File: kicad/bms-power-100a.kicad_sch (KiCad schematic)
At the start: 47 parts, among them P1 CONN_01X01, P2 CONN_01X01, P3 CONN_01X01, P4 CONN_01X01, Q1 Q_NMOS_GDS, Q10 Q_NMOS_GDS, Q11 Q_NMOS_GDS, Q12 Q_NMOS_GDS, Q13 Q_NMOS_GDS, Q14 Q_NMOS_GDS, Q15 Q_NMOS_GDS, Q16 Q_NMOS_GDS, Q17 Q_NMOS_GDS, Q18 Q_NMOS_GDS, Q19 Q_NMOS_GDS, Q2 Q_NMOS_GDS, Q20 Q_NMOS_GDS, Q21 ZXMP6A13F, Q3 Q_NMOS_GDS, Q4 Q_NMOS_GDS, Q5 Q_NMOS_GDS, Q6 Q_NMOS_GDS, Q7 Q_NMOS_GDS, Q8 Q_NMOS_GDS, Q9 Q_NMOS_GDS

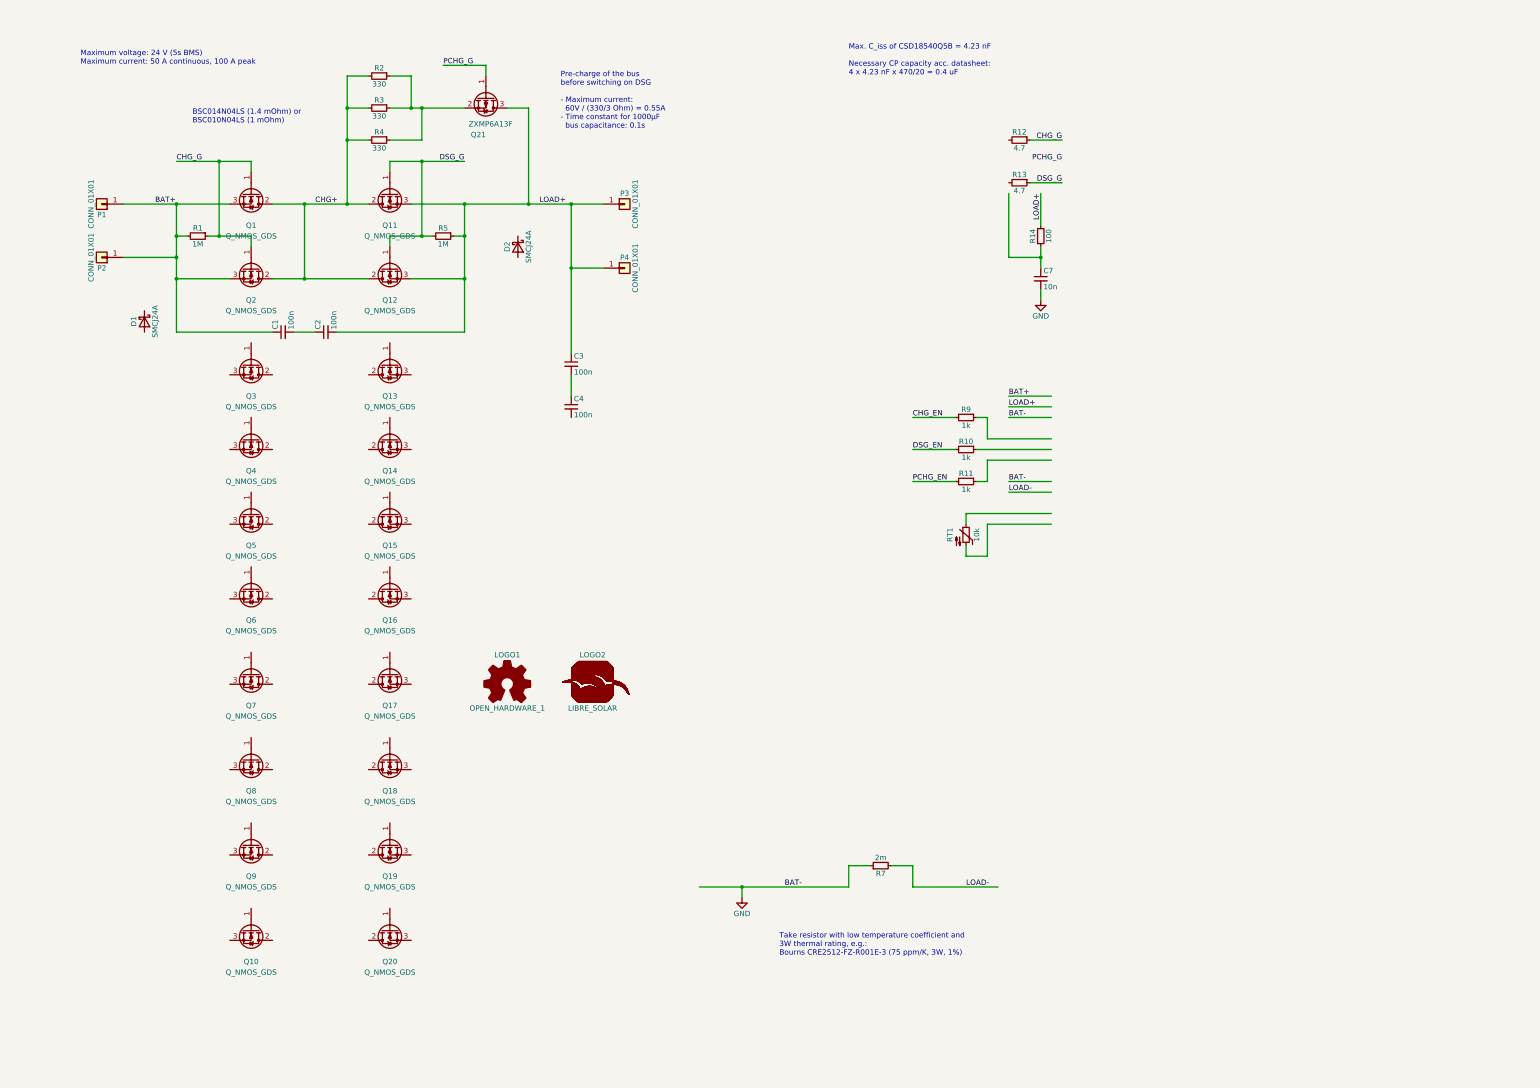
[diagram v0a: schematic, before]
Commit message: Update KiCad files based on spec updates
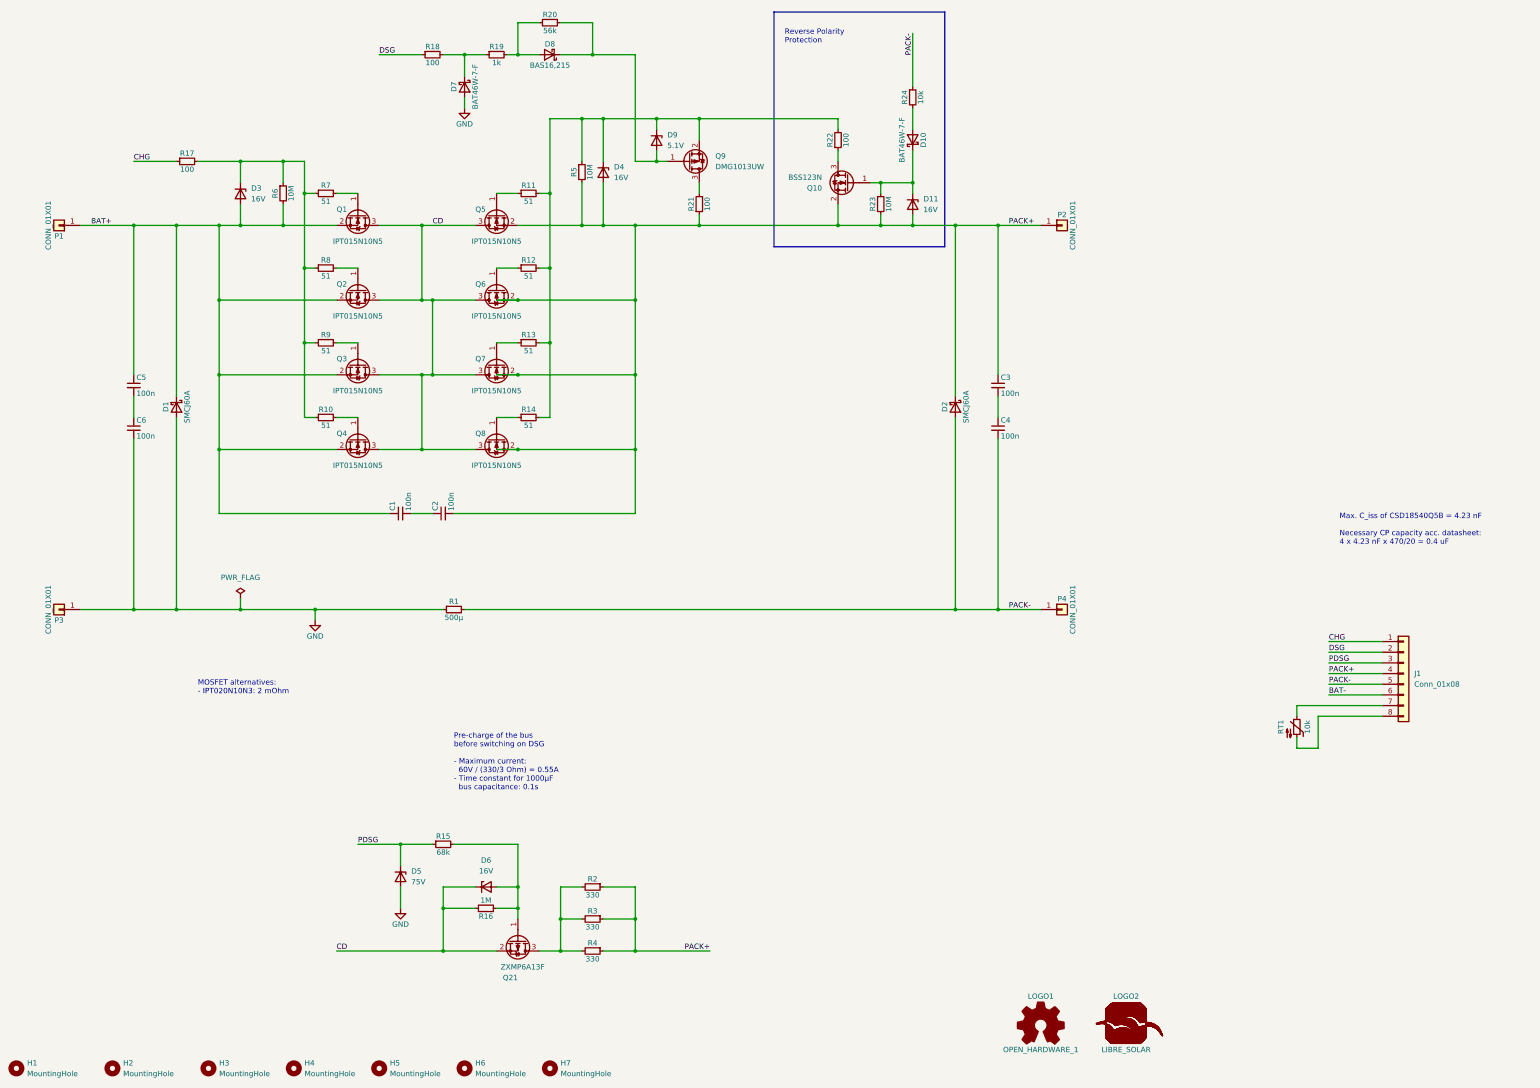
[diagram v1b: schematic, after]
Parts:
- removed C7: 10n, LibreSolar:C_0603_1608, symbol LibreSolar:C
- removed Q10, Q15, Q16, Q17, Q18, Q19, Q20, Q5, Q6, Q7, Q8, Q9: Q_NMOS_GDS, LibreSolar:TO-220-3_Horizontal_TabUp_NoHole, symbol Device:Q_NMOS_GDS
- added C5, C6: 100n, LibreSolar:C_0603_1608, symbol LibreSolar:C
- added D10, D7: BAT46W-7-F, LibreSolar:D_SOD-123, symbol LibreSolar:D_Schottky
- added D11, D3, D4, D6: 16V, LibreSolar:D_SOD-123, symbol LibreSolar:D_Zener
- added D5: 75V, LibreSolar:D_SOD-123, symbol LibreSolar:D_Zener
- added D8: BAS16,215, Diode_SMD:D_SOT-23_ANK, symbol LibreSolar:D_Schottky
- added D9: 5.1V, LibreSolar:D_SOD-323, symbol LibreSolar:D_Zener
- added H1, H2, H3, H4, H5, H6, H7: MountingHole, MountingHole:MountingHole_3.2mm_M3_ISO7380_Pad, symbol Mechanical:MountingHole
- added J1: Conn_01x08, Connector_PinSocket_2.54mm:PinSocket_1x08_P2.54mm_Vertical_SMD_Pin1Right, symbol Connector_Generic:Conn_01x08
- added Q10: BSS123N, Package_TO_SOT_SMD:SOT-23, symbol Device:Q_NMOS_GSD
- added Q9: DMG1013UW, Package_TO_SOT_SMD:SOT-323_SC-70, symbol Device:Q_PMOS_GSD
- added R15: 68k, LibreSolar:R_0603_1608, symbol LibreSolar:R
- added R16: 1M, LibreSolar:R_0603_1608, symbol LibreSolar:R
- added R17, R18, R21, R22: 100, LibreSolar:R_0603_1608, symbol LibreSolar:R
- added R19: 1k, LibreSolar:R_0603_1608, symbol LibreSolar:R
- added R20: 56k, LibreSolar:R_0603_1608, symbol LibreSolar:R
- added R23: 10M, LibreSolar:R_0603_1608, symbol LibreSolar:R
- added R24: 10k, LibreSolar:R_0603_1608, symbol LibreSolar:R
- added R7, R8: 51, LibreSolar:R_0603_1608, symbol LibreSolar:R
- D1, D2: value SMCJ24A -> SMCJ60A; Alternative (none) -> Diodes Inc. SMCJ60A-13-F; PartNumber SMCJ24A -> SMCJ60A
- P1, P2: footprint LibreSolar:Wuerth_WP-BUCF_7460408 -> LibreSolar:Busbar_100A_Wide
- P3, P4: footprint LibreSolar:Wuerth_WP-BUCF_7460408 -> LibreSolar:Busbar_100A_Short
- Q1, Q2, Q3, Q4: value Q_NMOS_GDS -> IPT015N10N5; footprint LibreSolar:TO-220-3_Horizontal_TabUp_NoHole -> Package_TO_SOT_SMD:Infineon_PG-HSOF-8-1_ThermalVias; symbol Device:Q_NMOS_GDS -> Device:Q_NMOS_GSD
- Q5: renamed from Q11; value Q_NMOS_GDS -> IPT015N10N5; footprint LibreSolar:TO-220-3_Horizontal_TabUp_NoHole -> Package_TO_SOT_SMD:Infineon_PG-HSOF-8-1_ThermalVias; symbol Device:Q_NMOS_GDS -> Device:Q_NMOS_GSD
- Q6: renamed from Q12; value Q_NMOS_GDS -> IPT015N10N5; footprint LibreSolar:TO-220-3_Horizontal_TabUp_NoHole -> Package_TO_SOT_SMD:Infineon_PG-HSOF-8-1_ThermalVias; symbol Device:Q_NMOS_GDS -> Device:Q_NMOS_GSD
- Q7: renamed from Q13; value Q_NMOS_GDS -> IPT015N10N5; footprint LibreSolar:TO-220-3_Horizontal_TabUp_NoHole -> Package_TO_SOT_SMD:Infineon_PG-HSOF-8-1_ThermalVias; symbol Device:Q_NMOS_GDS -> Device:Q_NMOS_GSD
- Q8: renamed from Q14; value Q_NMOS_GDS -> IPT015N10N5; footprint LibreSolar:TO-220-3_Horizontal_TabUp_NoHole -> Package_TO_SOT_SMD:Infineon_PG-HSOF-8-1_ThermalVias; symbol Device:Q_NMOS_GDS -> Device:Q_NMOS_GSD
- R1: renamed from R7; value 2m -> 500µ; footprint LibreSolar:R_Shunt_Vishay_WSMS5515 -> LibreSolar:R_Shunt_3920; Alternative (none) -> Bourns CSS2H-3920R-L500F; Manufacturer Bourns -> KOA Speer; PartNumber CRE2512-FZ-R002E-3 -> PSJ2NTEBL500F
- R10, R11, R9: value 1k -> 51; Manufacturer Yageo -> any; PartNumber RC0603FR-071KL -> (none)
- R12, R13: value 4.7 -> 51; Manufacturer Yageo -> any; PartNumber RC0603FR-074R7L -> (none)
- R14: value 100 -> 51; Manufacturer Yageo -> any; PartNumber RC0603FR-07100RL -> (none)
- R5: value 1M -> 10M
- R6: renamed from R1; value 1M -> 10M
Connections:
- net CHG_EN is gone; now on an unnamed net: R9.2
- net DSG_EN is gone; now on an unnamed net: R10.2
- net LOAD- is gone; now on net PACK-: R1.2
- net PCHG_EN is gone; now on an unnamed net: R11.2
- net BAT+: now also D1.1 (K), Q1.2 (S), Q2.2 (S), Q3.2 (S), Q4.2 (S), C5.1, D3.2 (A); no longer P2.1 (Pin_1), Q1.3 (S), Q2.3 (S)
- net GND: now also D1.2 (A), P3.1 (Pin_1), C6.2, D5.2 (A), D7.2 (A)
- net at R9.1: now also R10.1, R6.1, D3.1 (K), R17.2, R7.1, R8.1
- net at R11.1: now also Q5.1 (G)
- net at RT1.1: now also J1.7 (Pin_7)
- net at RT1.2: now also J1.8 (Pin_8)
- net PACK+: now reaches D2.1 (K)
- net PACK+: now also C2.2, C3.1, P2.1 (Pin_1), Q5.2 (S), Q6.2 (S), Q7.2 (S), Q8.2 (S), R2.1, R3.1, R4.1, R5.2, D11.2 (A), D4.2 (A), J1.4 (Pin_4), Q10.2 (S), R21.1, R23.2
- net PACK-: now reaches D2.2 (A)
- net PACK-: now also C4.2, P4.1 (Pin_1), J1.5 (Pin_5), R24.1
- net at R12.2: now also R13.2, R14.2, R5.1, D4.1 (K), D9.1 (K), Q9.2 (S), R22.2
- net at R14.1: now also Q8.1 (G)
- net CD: now reaches Q4.3 (D)
- net CD: now also Q1.3 (D), Q2.3 (D), Q21.2 (S), Q3.3 (D), Q5.3 (D), Q6.3 (D), Q7.3 (D), Q8.3 (D), D6.1 (K), R16.1
- net at Q7.1 (G): now also R13.1
- removed net CHG+: Q1.2 (D), Q2.2 (D), Q5.2 (D), Q6.2 (D), R2.2, R3.2, R4.2
- removed net CHG_G: Q1.1 (G), Q2.1 (G), R12.1, R6.1
- removed net DSG_G: Q5.1 (G), Q6.1 (G), R13.1, R5.2
- removed net LOAD+: C2.2, C3.1, P3.1 (Pin_1), P4.1 (Pin_1), Q21.3 (D), Q5.3 (S), Q6.3 (S), R14.2, R5.1
- net PCHG_G: no longer names the net of Q21.1 (G)
- net PCHG_G: now also D6.2 (A), R15.2, R16.2
- new net: Q21.3 (D), R2.2, R3.2, R4.2
- new net: D10.2 (A), R24.2
- new net: Q2.1 (G), R8.2
- new net: D8.1 (K), D9.2 (A), Q9.1 (G), R20.2
- new net: Q9.3 (D), R21.2
- new net: D7.1 (K), R18.2, R19.1
- new net: C5.2, C6.1
- new net: D10.1 (K), D11.1 (K), Q10.1 (G), R23.1
- new net: Q10.3 (D), R22.1
- new net: Q1.1 (G), R7.2
- new net: D8.2 (A), R19.2, R20.1
- new net: Q6.1 (G), R12.1
- new net BAT-: J1.6 (Pin_6)
- new net CHG: J1.1 (Pin_1), R17.1
- new net DSG: J1.2 (Pin_2), R18.1
- new net PDSG: D5.1 (K), J1.3 (Pin_3), R15.1
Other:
- note added: "MOSFET alternatives: - IPT020N10N3: 2 mOhm"
- note added: "Reverse Polarity Protection"
- note removed: "BSC014N04LS (1.4 mOhm) or BSC010N04LS (1 mOhm)"
- note removed: "Maximum voltage: 24 V (5s BMS) Maximum current: 50 A continuous, 100 A peak"
- note removed: "Take resistor with low temperature coefficient and 3W thermal rating, e.g.: Bourns CRE2512-FZ-R001E-3 (75 ppm/K, 3W, 1%)"
- moved on the sheet: C1, C2, C3, C4, D1, D2, LOGO1, LOGO2, P1, P2, Q1, Q2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

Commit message: WIP: Schematic almost finished
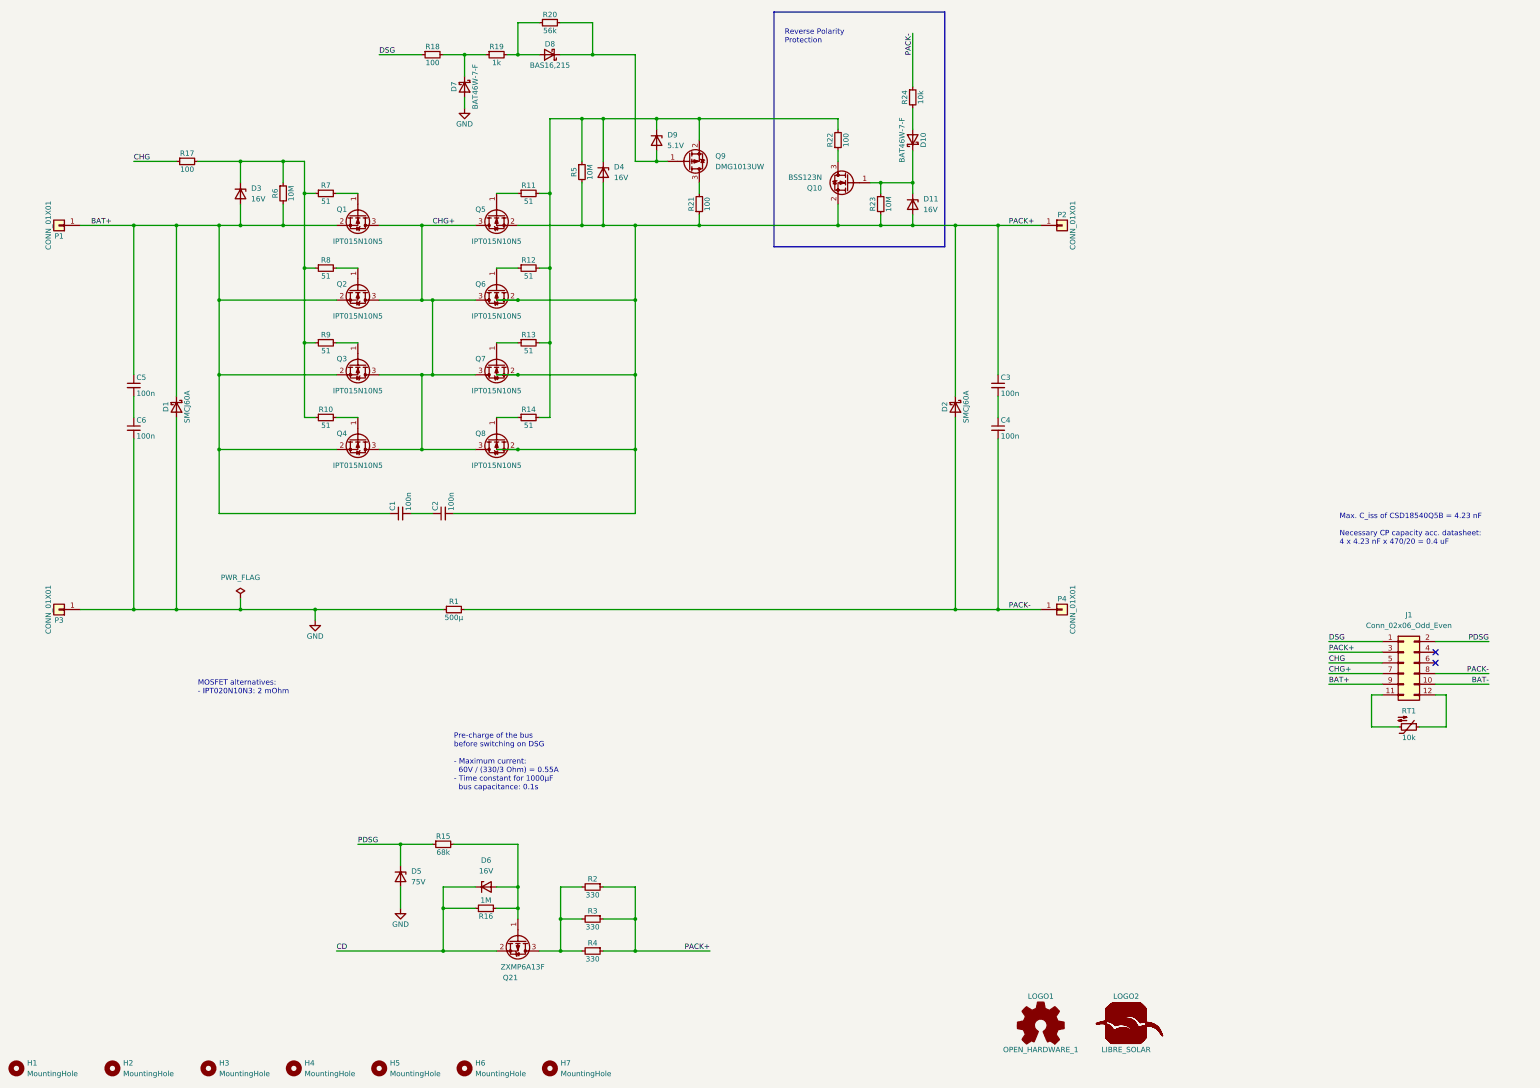
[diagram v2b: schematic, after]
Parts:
- removed J1: Conn_01x08, Connector_PinSocket_2.54mm:PinSocket_1x08_P2.54mm_Vertical_SMD_Pin1Right, symbol Connector_Generic:Conn_01x08
- added J1: Conn_02x06_Odd_Even, Connector_PinHeader_2.54mm:PinHeader_2x06_P2.54mm_Vertical_SMD, symbol Connector_Generic:Conn_02x06_Odd_Even
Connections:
- net BAT+: now also J1.9 (Pin_9)
- net BAT-: now also J1.10 (Pin_10)
- net CD: no longer Q1.3 (D), Q2.3 (D), Q3.3 (D), Q4.3 (D), Q5.3 (D), Q6.3 (D), Q7.3 (D), Q8.3 (D)
- net CHG: now also J1.5 (Pin_5)
- net DSG: now also J1.1 (Pin_1)
- net PACK+: now also J1.3 (Pin_3)
- net PACK-: now also J1.8 (Pin_8)
- net PDSG: now also J1.2 (Pin_2)
- net at RT1.1: now also J1.12 (Pin_12)
- net at RT1.2: now also J1.11 (Pin_11)
- new net CHG+: J1.7 (Pin_7), Q1.3 (D), Q2.3 (D), Q3.3 (D), Q4.3 (D), Q5.3 (D), Q6.3 (D), Q7.3 (D), Q8.3 (D)
- no-connect marks 0 -> 2
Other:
- moved on the sheet: RT1

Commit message: v0.1 design ready for review
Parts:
- removed H7: MountingHole, MountingHole:MountingHole_3.2mm_M3_ISO7380_Pad, symbol Mechanical:MountingHole
- removed J1: Conn_02x06_Odd_Even, Connector_PinHeader_2.54mm:PinHeader_2x06_P2.54mm_Vertical_SMD, symbol Connector_Generic:Conn_02x06_Odd_Even
- removed R2, R3, R4: 330, LibreSolar:R_2010_5025, symbol LibreSolar:R
- added FID1, FID2: Fiducial, Fiducial:Fiducial_1mm_Mask2mm, symbol Mechanical:Fiducial
- added J1, J2: Conn_01x06, Connector_PinHeader_2.00mm:PinHeader_1x06_P2.00mm_Vertical_SMD_Pin1Left, symbol Connector_Generic:Conn_01x06
- added R2: 40, Package_TO_SOT_SMD:TO-252-2, symbol Device:R_Potentiometer_Trim
- C1, C2, C3, C4, C5, C6: Manufacturer Yageo -> any; PartNumber CC0603KRX7R9BB104 -> (none); Remarks (none) -> X7R, 100V
- D1, D2: Alternative Diodes Inc. SMCJ60A-13-F -> (none); Remarks (none) -> Alternative: Diodes Inc. SMCJ60A-13-F
- P1, P2: footprint LibreSolar:Busbar_100A_Wide -> LibreSolar:Busbar_100A_Long_Stud; Manufacturer Wuerth -> Custom; PartNumber 74650195 -> (none)
- P3, P4: footprint LibreSolar:Busbar_100A_Short -> LibreSolar:Busbar_100A_Short_Stud; Manufacturer Wuerth -> Custom; PartNumber 74650195 -> (none)
- Q1, Q2, Q3, Q4, Q5, Q6, Q7, Q8: Manufacturer (none) -> Infineon; PartNumber (none) -> IPT015N10N5; Remarks (none) -> Alternative with 2mOhm: IPT020N10N3
- Q10: Manufacturer (none) -> any; PartNumber (none) -> BSS123N
- R1: Alternative Bourns CSS2H-3920R-L500F -> (none); Remarks (none) -> Alternative: Bourns CSS2H-3920R-L500F
- R10, R11, R12, R13, R14, R7, R8, R9: value 51 -> 47
- R16, R23, R24, R5, R6: Manufacturer Yageo -> any; PartNumber RC0603FR-071ML -> (none)
- R20: value 56k -> 68k
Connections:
- net CD is gone; now on net CHG+: D6.1 (K), Q21.2 (S), R16.1
- net BAT+: now also J2.1 (Pin_1)
- net CHG: now also J2.3 (Pin_3)
- net CHG+: now also J2.4 (Pin_4), R2.2
- net DSG: now also J1.4 (Pin_4)
- net GND: now also J1.5 (Pin_5), J2.2 (Pin_2)
- net PACK+: now also J1.1 (Pin_1), R2.3
- net PACK-: now also J1.6 (Pin_6)
- net PDSG: now also J1.3 (Pin_3)
- net at RT1.1: now also J2.5 (Pin_5)
- net at RT1.2: now also J2.6 (Pin_6)
- net at Q21.3 (D): now also R2.1
- net CHG_G: now reaches D3.1 (K), R10.1, R17.2, R6.1, R7.1, R8.1, R9.1
- net DSG_G: now reaches D4.1 (K), D9.1 (K), Q9.2 (S), R11.2, R12.2, R13.2, R14.2, R22.2, R5.1
- no-connect marks 2 -> 1
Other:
- note added: "BAT-"
- note added: "Control board power supply"
- note added: "Current sensor Kelvin connection"
- note added: "Libre Solar BMS 16S100 SC - Power Part"
- note added: "Pre-charge of the bus before switching on DSG - Maximum current: 60V / 40R = 1.5A - Time constant for 5000µF bus capacitance: 0.2s - Dissipated energy: 9J"
- note removed: "Max. C_iss of CSD18540Q5B = 4.23 nF Necessary CP capacity acc. datasheet: 4 x 4.23 nF x 470/20 = 0.4 uF"
- note removed: "Pre-charge of the bus before switching on DSG - Maximum current: 60V / (330/3 Ohm) = 0.55A - Time constant for 1000µF bus capacitance: 0.1s"
- company: (none) -> Libre Solar Technologies GmbH
- title: (none) -> BMS 16S Power PCB
- moved on the sheet: C1, C2, C3, C4, C5, C6, D1, D10, D11, D2, D3, D4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
